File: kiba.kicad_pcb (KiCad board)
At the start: 2 copper layers, 56.5 x 65 mm, 61 parts, among them IC1 SHT40-CD1B-R3, IC2 SGP40-D-R4, IC3 SGP40-D-R4, IC4 SGP40-D-R4, IC6 SGP40-D-R4, J1 Raspberry_Pi_2_3, Q1 2N7002NXAKR, U1 LM1117MP-3.3, U2 TCA9546APWR, U3 BMP581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

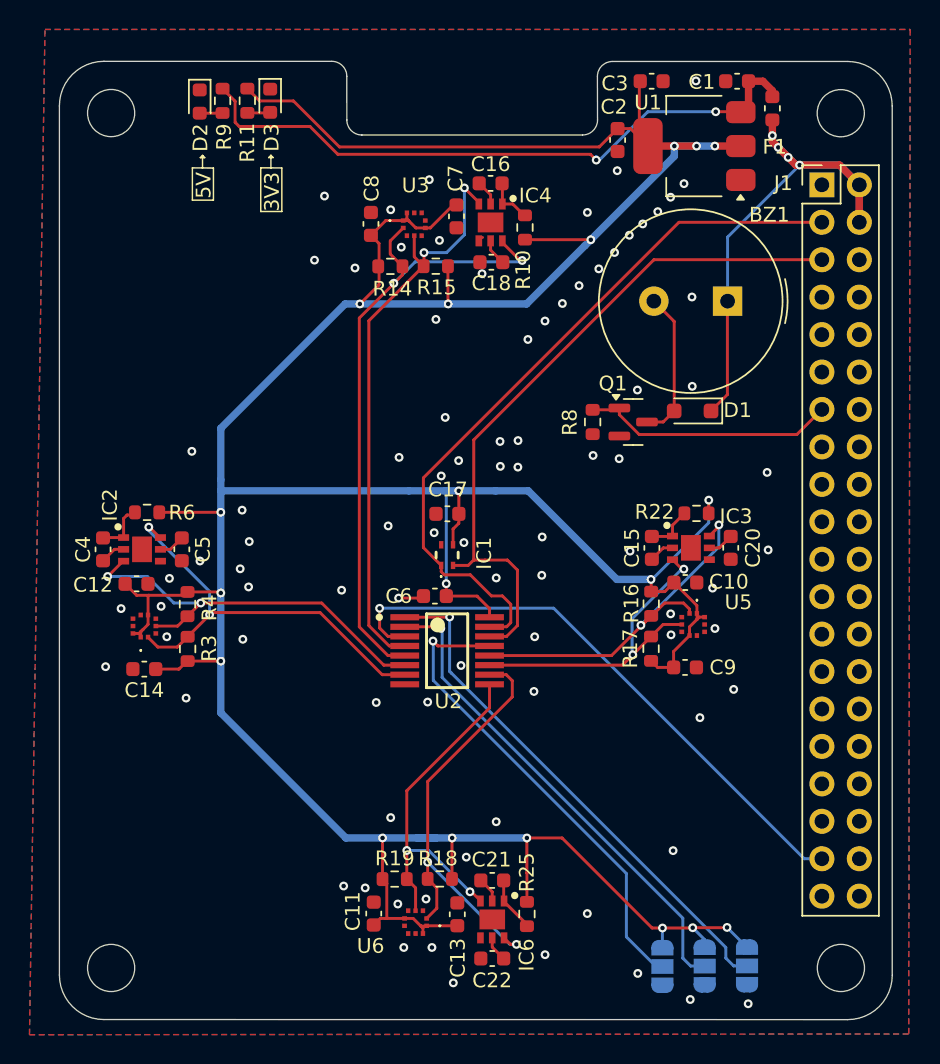
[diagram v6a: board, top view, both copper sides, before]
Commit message: fix: pullup resistors layout
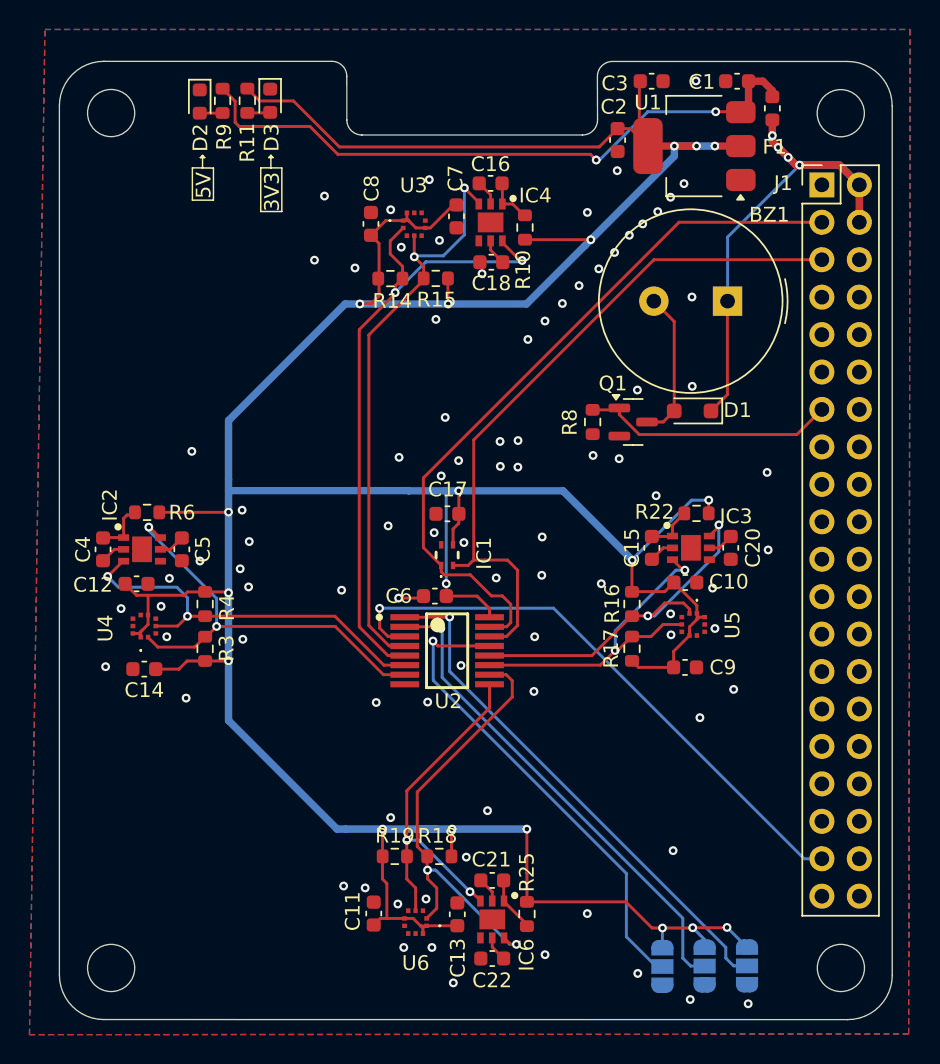
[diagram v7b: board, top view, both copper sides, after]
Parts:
- moved R19 1.54 mm to (138.3, 123.7)
- moved R18 1.53 mm to (141.3, 123.7)
- moved R16 1.31 mm to (154.4, 106.5)
- moved R17 1.30 mm to (154.4, 109.6)
- moved R4 1.20 mm to (125.5, 106.5)
- moved R3 1.19 mm to (125.5, 109.6)
- moved R14 0.83 mm to (138.0, 84.5)
- moved R15 0.83 mm to (141.1, 84.4)
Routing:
- net /Sensors/SCK_2: track 26.5 -> 25.0 mm
- net +3V3: track 276.0 -> 276.5 mm
- net /Sensors/SDA_1: track 27.9 -> 27.3 mm
- net GND: track 1.80 -> 1.74 mm, vias 87 -> 88

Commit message: Added JLCPCB part numbers and generated BOM
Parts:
- added R1: 10k, Resistor_SMD:R_0603_1608Metric, F.Cu at (138.3, 104.5)
- R14, R15, R16, R17, R18, R19, R3, R4: value R -> 2k2
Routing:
- net +3V3: track 276.5 -> 279.5 mm
- net /~{RESET}: track 40.3 -> 42.7 mm
